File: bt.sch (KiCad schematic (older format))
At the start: 3 parts, among them J5 RN52_BREAKOUT, P1 CONN_01X06

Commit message: Correct footprints for caps and DB15s
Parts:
- C1: footprint Capacitors_THT:C_Disc_D5.0mm_W2.5mm_P2.50mm -> blubaru:C_Disc_D5.5mm_W2.5mm_P2.50mm
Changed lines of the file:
@@
 F 0 "C1" H 5125 5350 50  0000 L CNN
 F 1 "0.1uF" H 5125 5150 50  0000 L CNN
-F 2 "Capacitors_THT:C_Disc_D5.0mm_W2.5mm_P2.50mm" H 5138 5100 50  0001 C CNN
-F 3 "" H 5100 5250 50  0000 C CNN
+F 2 "blubaru:C_Disc_D5.5mm_W2.5mm_P2.50mm" H 5138 5100 50  0001 C CNN
+F 3 "https://product.tdk.com/info/en/documents/spec/leadmlccspec_conventional_en.pdf" H 5100 5250 50  0001 C CNN
 	1    5100 5250
 	0    1    1    0

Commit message: Add a line_driver schematic
This branch contains the full line driver with 2nd order filter, which
provides a low-pass filter on the input.
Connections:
- net Amp/L+ renamed Line Driver/L+
- net Amp/L- renamed Line Driver/L-
- net Amp/R+ renamed Line Driver/R+
- net Amp/R- renamed Line Driver/R-
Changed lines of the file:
@@
 $EndComp
 $Comp
-L GND #PWR017
+L GND #PWR018
 U 1 1 589AA392
 P 5800 5250
-F 0 "#PWR017" H 5800 5000 50  0001 C CNN
+F 0 "#PWR018" H 5800 5000 50  0001 C CNN
 F 1 "GND" H 5800 5100 50  0000 C CNN
 F 2 "" H 5800 5250 50  0000 C CNN
@@
 $EndComp
 $Comp
-L VCC #PWR018
+L VCC #PWR019
 U 1 1 589AA3E5
 P 4400 5250
-F 0 "#PWR018" H 4400 5100 50  0001 C CNN
+F 0 "#PWR019" H 4400 5100 50  0001 C CNN
 F 1 "VCC" H 4400 5400 50  0000 C CNN
 F 2 "" H 4400 5250 50  0000 C CNN
@@
 $EndComp
 $Comp
-L GND #PWR019
+L GND #PWR020
 U 1 1 589E813D
 P 3950 3350
-F 0 "#PWR019" H 3950 3100 50  0001 C CNN
+F 0 "#PWR020" H 3950 3100 50  0001 C CNN
 F 1 "GND" H 3950 3200 50  0000 C CNN
 F 2 "" H 3950 3350 50  0000 C CNN
@@
 F5 "MIC_L+" O L 7000 4300 60
 F6 "MIC_BIAS" O L 7000 4400 60
-$EndSheet
-$Sheet
-S 6700 2950 1100 500
-U 58AE00D8
-F0 "Amp" 60
-F1 "amp.sch" 60
-F2 "LineOutL" O R 7800 3050 60
-F3 "LineOutR" O R 7800 3150 60
-F4 "L+" I L 6700 3050 60
-F5 "R+" I L 6700 3150 60
-F6 "L-" I L 6700 3250 60
-F7 "R-" I L 6700 3350 60
 $EndSheet
 Text HLabel 8150 3050 2    60   Output ~ 0
@@
 Wire Wire Line
 	6150 4400 7000 4400
+$Sheet
+S 6700 2950 1100 500
+U 590D0DAE
+F0 "Line Driver" 60
+F1 "line_driver.sch" 60
+F2 "LineOutR" O R 7800 3150 60
+F3 "LineOutL" O R 7800 3050 60
+F4 "L-" I L 6700 3250 60
+F5 "L+" I L 6700 3050 60
+F6 "R-" I L 6700 3350 60
+F7 "R+" I L 6700 3150 60
+$EndSheet
 $EndSCHEMATC

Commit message: Add resistor values to LEDs and a voltage regulator. Has power pin errors still.
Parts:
- renumbered C1 to C3
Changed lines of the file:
@@
 $EndComp
 $Comp
-L GND #PWR21
+L GND #PWR023
 U 1 1 589AA392
 P 5800 5250
-F 0 "#PWR21" H 5800 5000 50  0001 C CNN
+F 0 "#PWR023" H 5800 5000 50  0001 C CNN
 F 1 "GND" H 5800 5100 50  0000 C CNN
 F 2 "" H 5800 5250 50  0000 C CNN
@@
 $EndComp
 $Comp
-L VCC #PWR20
+L VCC #PWR024
 U 1 1 589AA3E5
 P 4400 5250
-F 0 "#PWR20" H 4400 5100 50  0001 C CNN
+F 0 "#PWR024" H 4400 5100 50  0001 C CNN
 F 1 "VCC" H 4400 5400 50  0000 C CNN
 F 2 "" H 4400 5250 50  0000 C CNN
@@
 NoConn ~ 5800 3950
 $Comp
-L C C1
+L C C3
 U 1 1 589BA198
 P 5100 5250
-F 0 "C1" H 5125 5350 50  0000 L CNN
+F 0 "C3" H 5125 5350 50  0000 L CNN
 F 1 "0.1uF" H 5125 5150 50  0000 L CNN
 F 2 "blubaru:C_Disc_D5.5mm_W2.5mm_P2.50mm" H 5138 5100 50  0001 C CNN
@@
 $EndComp
 $Comp
-L GND #PWR19
+L GND #PWR025
 U 1 1 589E813D
 P 3950 3350
-F 0 "#PWR19" H 3950 3100 50  0001 C CNN
+F 0 "#PWR025" H 3950 3100 50  0001 C CNN
 F 1 "GND" H 3950 3200 50  0000 C CNN
 F 2 "" H 3950 3350 50  0000 C CNN

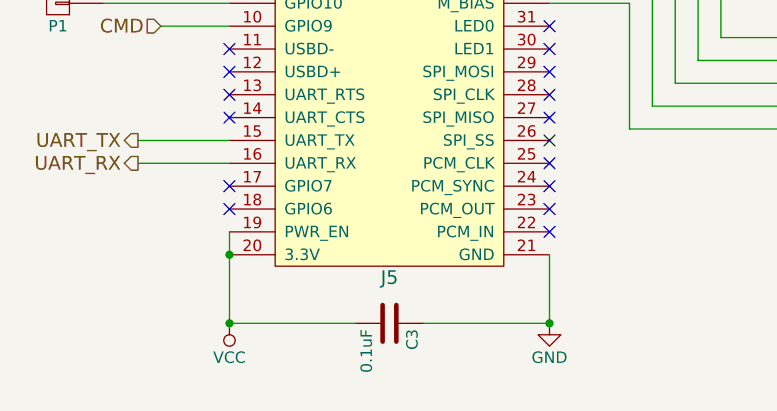
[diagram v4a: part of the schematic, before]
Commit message: Voltage regulator adjustments and tidying
Switch to LD1117 component and add decoupling caps.
Add a decoupling cap to the audio switch
Shift some status LEDs to modules layer
Use ProMini instead of ProMicro
Update BOM
Update netlist
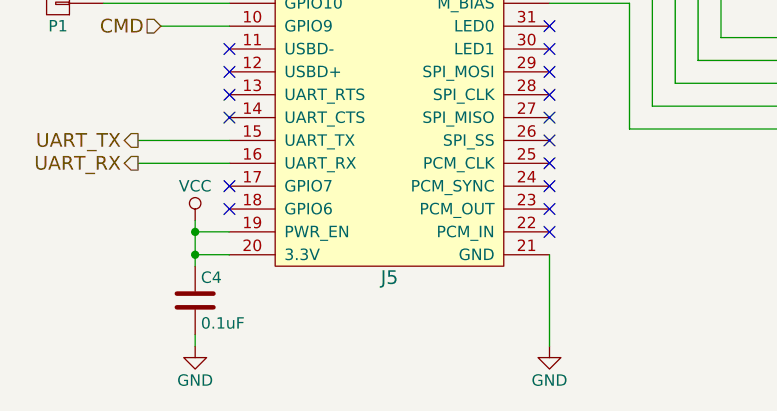
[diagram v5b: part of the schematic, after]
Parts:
- renumbered C3 to C4
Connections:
- net GND: now also C4.2; no longer C4.1
- net VCC: now also C4.1; no longer C4.2
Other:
- moved on the sheet: C4
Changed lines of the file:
@@
 $EndComp
 $Comp
-L GND #PWR023
+L GND #PWR022
 U 1 1 589AA392
-P 5800 5250
-F 0 "#PWR023" H 5800 5000 50  0001 C CNN
-F 1 "GND" H 5800 5100 50  0000 C CNN
-F 2 "" H 5800 5250 50  0000 C CNN
-F 3 "" H 5800 5250 50  0000 C CNN
-	1    5800 5250
-	1    0    0    -1
-$EndComp
-$Comp
-L VCC #PWR024
+P 5800 5350
+F 0 "#PWR022" H 5800 5100 50  0001 C CNN
+F 1 "GND" H 5800 5200 50  0000 C CNN
+F 2 "" H 5800 5350 50  0000 C CNN
+F 3 "" H 5800 5350 50  0000 C CNN
+	1    5800 5350
+	1    0    0    -1
+$EndComp
+$Comp
+L VCC #PWR023
 U 1 1 589AA3E5
-P 4400 5250
-F 0 "#PWR024" H 4400 5100 50  0001 C CNN
-F 1 "VCC" H 4400 5400 50  0000 C CNN
-F 2 "" H 4400 5250 50  0000 C CNN
-F 3 "" H 4400 5250 50  0000 C CNN
-	1    4400 5250
-	-1   0    0    1
+P 4250 4800
+F 0 "#PWR023" H 4250 4650 50  0001 C CNN
+F 1 "VCC" H 4250 4950 50  0000 C CNN
+F 2 "" H 4250 4800 50  0000 C CNN
+F 3 "" H 4250 4800 50  0000 C CNN
+	1    4250 4800
+	1    0    0    -1
 $EndComp
 NoConn ~ 4400 3050
@@
 NoConn ~ 5800 3950
 $Comp
-L C C3
+L C C4
 U 1 1 589BA198
-P 5100 5250
-F 0 "C3" H 5125 5350 50  0000 L CNN
-F 1 "0.1uF" H 5125 5150 50  0000 L CNN
-F 2 "blubaru:C_Disc_D5.5mm_W2.5mm_P2.50mm" H 5138 5100 50  0001 C CNN
-F 3 "https://product.tdk.com/info/en/documents/spec/leadmlccspec_conventional_en.pdf" H 5100 5250 50  0001 C CNN
-	1    5100 5250
-	0    1    1    0
-$EndComp
-Wire Wire Line
-	4400 4850 4400 5250
+P 4250 5150
+F 0 "C4" H 4275 5250 50  0000 L CNN
+F 1 "0.1uF" H 4275 5050 50  0000 L CNN
+F 2 "blubaru:C_Disc_D5.5mm_W2.5mm_P2.50mm" H 4288 5000 50  0001 C CNN
+F 3 "https://product.tdk.com/info/en/documents/spec/leadmlccspec_conventional_en.pdf" H 4250 5150 50  0001 C CNN
+	1    4250 5150
+	1    0    0    -1
+$EndComp
 Wire Wire Line
 	3850 3450 4400 3450
@@
 Wire Wire Line
 	3850 3850 4400 3850
-Connection ~ 4400 4950
-Wire Wire Line
-	5800 4950 5800 5250
-Wire Wire Line
-	5800 5250 5250 5250
-Wire Wire Line
-	4400 5250 4950 5250
-Connection ~ 5800 5250
-Connection ~ 4400 5250
+Wire Wire Line
+	5800 4950 5800 5350
 $Comp
 L CONN_01X06 P1
@@
 $EndComp
 $Comp
-L GND #PWR025
+L GND #PWR024
 U 1 1 589E813D
 P 3950 3350
-F 0 "#PWR025" H 3950 3100 50  0001 C CNN
+F 0 "#PWR024" H 3950 3100 50  0001 C CNN
 F 1 "GND" H 3950 3200 50  0000 C CNN
 F 2 "" H 3950 3350 50  0000 C CNN
@@
 F7 "R+" I L 6700 3150 60
 $EndSheet
+Wire Wire Line
+	4400 4850 4250 4850
+Wire Wire Line
+	4250 4800 4250 5000
+Connection ~ 4250 4850
+Connection ~ 4250 4950
+Wire Wire Line
+	4250 4950 4400 4950
+$Comp
+L GND #PWR025
+U 1 1 594F3947
+P 4250 5350
+F 0 "#PWR025" H 4250 5100 50  0001 C CNN
+F 1 "GND" H 4250 5200 50  0000 C CNN
+F 2 "" H 4250 5350 50  0001 C CNN
+F 3 "" H 4250 5350 50  0001 C CNN
+	1    4250 5350
+	1    0    0    -1
+$EndComp
+Wire Wire Line
+	4250 5300 4250 5350
 $EndSCHEMATC

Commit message: Add new capacitor footprints and associate them.
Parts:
- C4: footprint blubaru:C_Disc_D5.5mm_W2.5mm_P2.50mm -> blubaru:C_Disc_D4.0mm_W2.6mm_P2.50mm
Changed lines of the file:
@@
 F 0 "C4" H 4275 5250 50  0000 L CNN
 F 1 "0.1uF" H 4275 5050 50  0000 L CNN
-F 2 "blubaru:C_Disc_D5.5mm_W2.5mm_P2.50mm" H 4288 5000 50  0001 C CNN
+F 2 "blubaru:C_Disc_D4.0mm_W2.6mm_P2.50mm" H 4288 5000 50  0001 C CNN
 F 3 "https://product.tdk.com/info/en/documents/spec/leadmlccspec_conventional_en.pdf" H 4250 5150 50  0001 C CNN
 	1    4250 5150
